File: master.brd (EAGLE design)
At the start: 160 x 100 mm, 24 parts, among them IC1 MEGA164P/324P/644P-PU, SW1 CI-11, U2 3V3 something

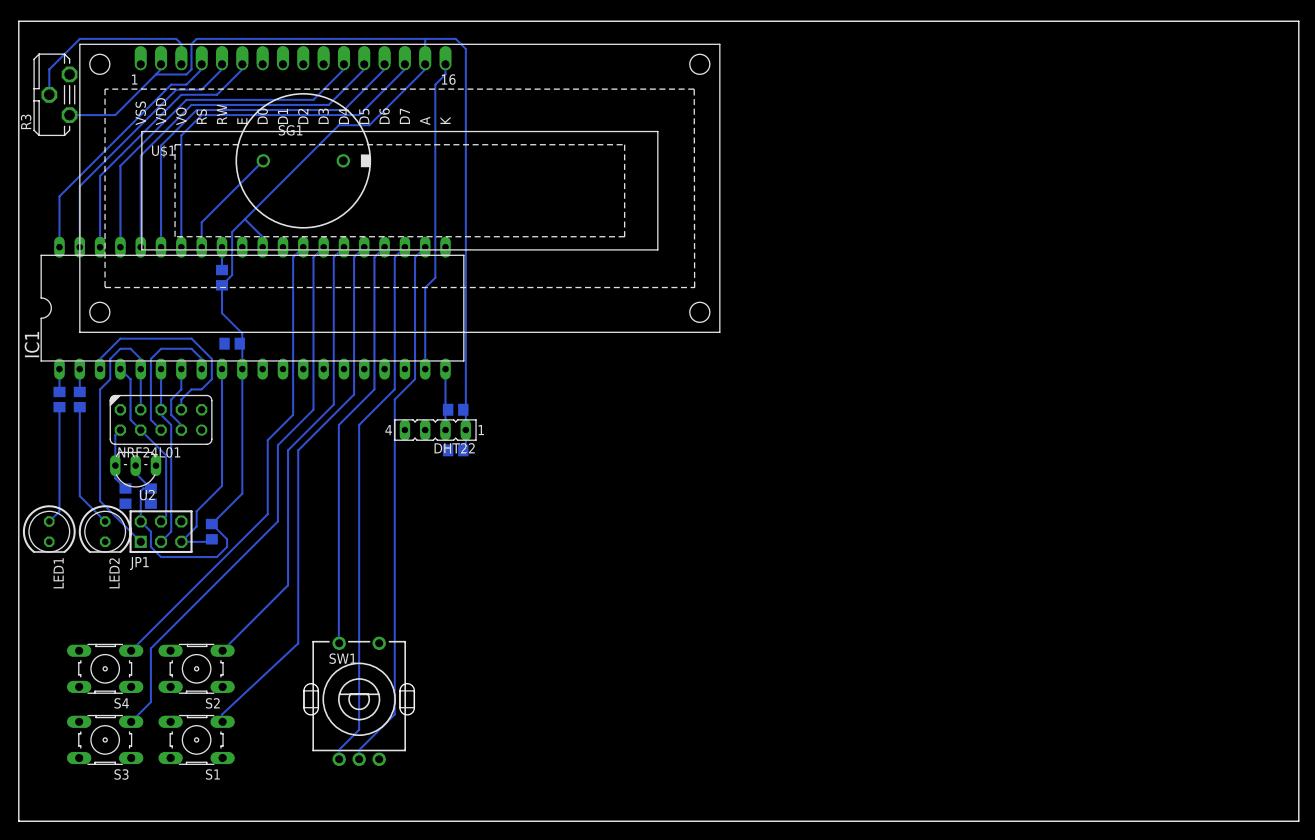
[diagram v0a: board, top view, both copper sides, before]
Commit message: added watch crystal to master, notes for sensor
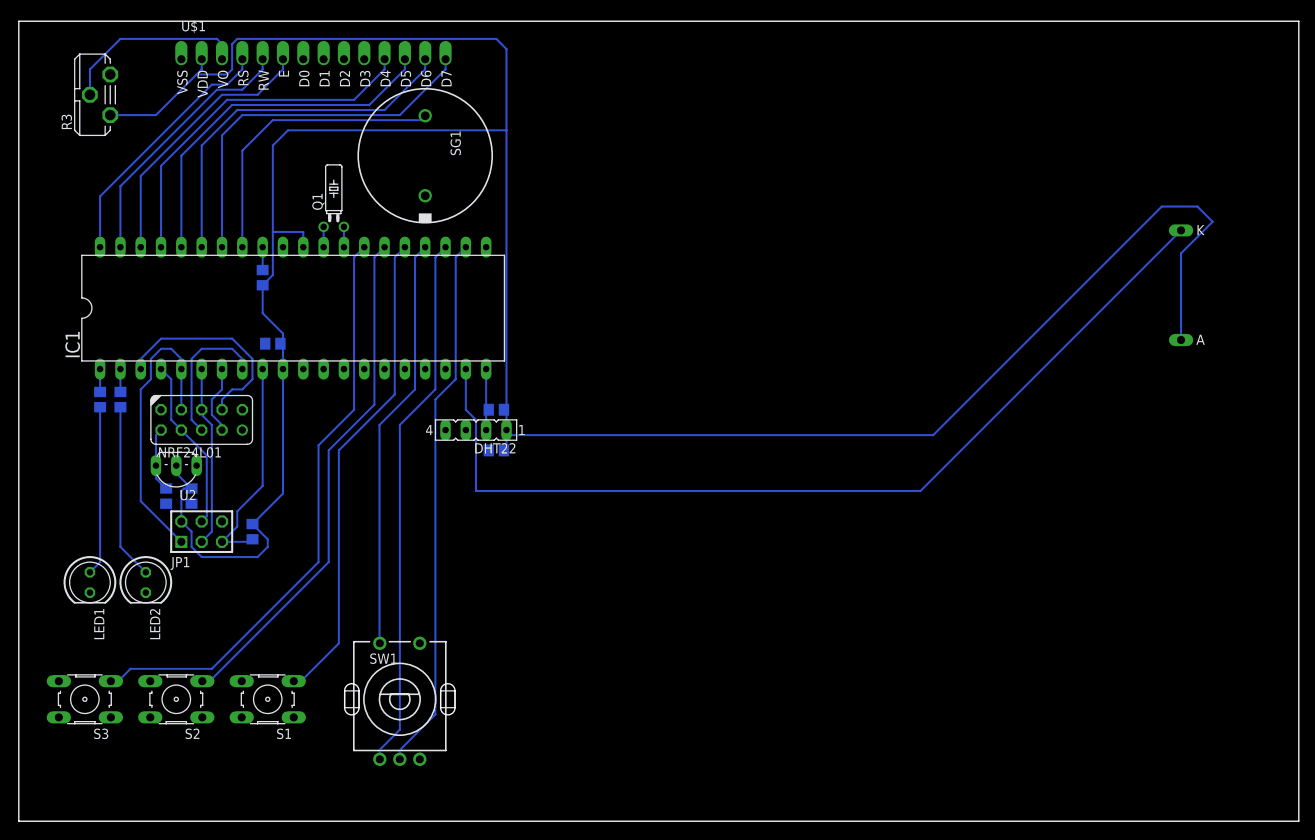
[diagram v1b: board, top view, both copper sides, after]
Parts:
- removed S4: (no value), switch-omron:B3F-10XX
- added Q1: (no value), crystal:TC26H
- U$1: value 162A -> BTHQ24008VSS; device lcd_displays:162A -> lcd_displays:BTHQ42008VSS
- moved SG1 15.3 mm to (50.8, 83.2), turned to 270 degrees
- moved S1 10.2 mm to (31.1, 15.2)
- moved U$1 8.26 mm to (2.54, 97.8)
- moved LED1 8.13 mm to (8.89, 29.8)
- moved LED2 8.13 mm to (15.9, 29.8)
- moved S3 5.68 mm to (8.26, 15.2)
- moved C2 5.08 mm to (30.5, 67.9)
- moved R1 5.08 mm to (29.2, 36.2)
- moved R3 5.08 mm to (10.2, 90.8)
- moved R4 5.08 mm to (10.2, 52.7)
- moved R5 5.08 mm to (12.7, 52.7)
- moved C1 5.08 mm to (31.8, 59.7)
- moved C3 5.08 mm to (59.7, 46.4)
- moved C7 5.08 mm to (21.6, 40.6)
- moved C8 5.08 mm to (18.4, 40.6)
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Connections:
- removed net PC6: IC1.28, S4.3
- new net N$3: IC1.29, Q1.1
- new net N$4: IC1.28, Q1.2
- net +5V: now also U$1.A, U$1.VDD; no longer U$1.15, U$1.2
- net GND: now also U$1.VSS; no longer S4.1, S4.2, U$1.1
- net N$9: now also U$1.VO; no longer U$1.3
- net PA0: now also U$1.RS; no longer U$1.4
- net PA1: now also U$1.RW; no longer U$1.5
- net PA2: now also U$1.E; no longer U$1.6
- net PA3: now also U$1.D4; no longer U$1.11
- net PA4: now also U$1.D5; no longer U$1.12
- net PA5: now also U$1.D6; no longer U$1.13
- net PA6: now also U$1.D7; no longer U$1.14
- net PD5: now also U$1.K; no longer U$1.16
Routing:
- net +5V: track 215.9 -> 339.6 mm
- net PD5: track 39.2 -> 117.4 mm
- net PC6: track 59.4 -> 0.00 mm
- net PA7: track 14.0 -> 36.7 mm
- net PC4: track 56.7 -> 64.2 mm
- net PC3: track 66.9 -> 60.5 mm
- net N$2: track 15.6 -> 22.0 mm
- net N$13: track 14.8 -> 21.2 mm
- net PC5: track 69.3 -> 73.9 mm
- net N$4: track 0.00 -> 2.54 mm
- net N$3: track 0.00 -> 2.54 mm
- net PA2: track 32.8 -> 33.5 mm
- net PA0: track 31.3 -> 32.0 mm
- net PA6: track 46.0 -> 46.6 mm
- net PA5: track 45.2 -> 45.9 mm
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
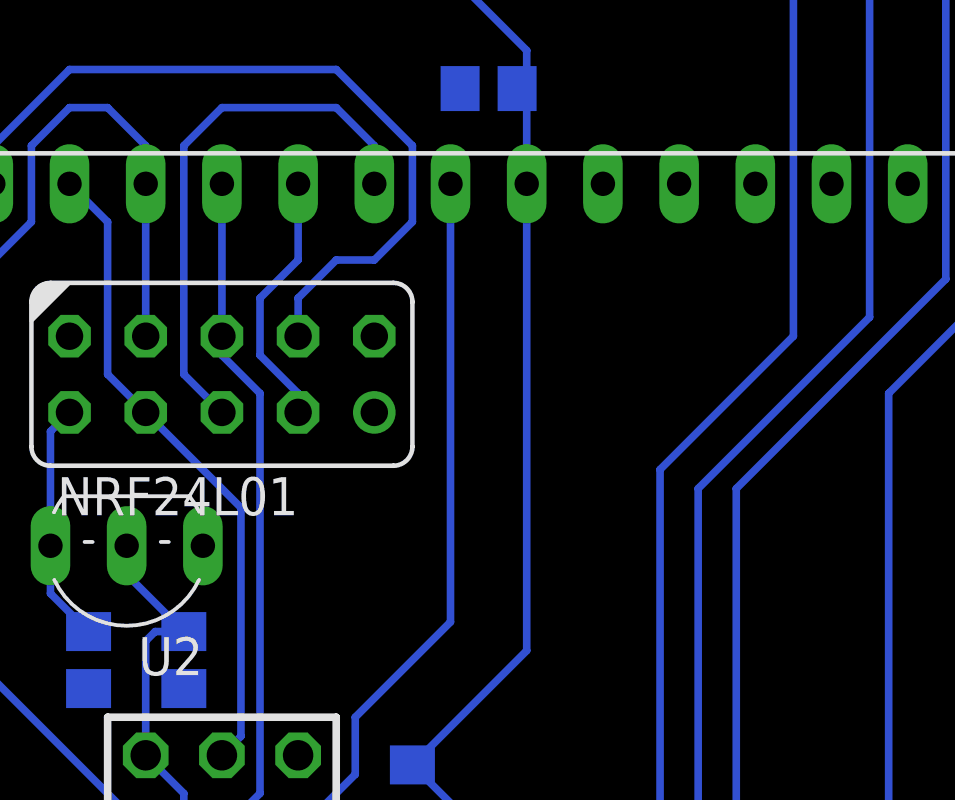
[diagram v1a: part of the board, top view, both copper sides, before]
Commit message: series resistors for shared spi/isp interface
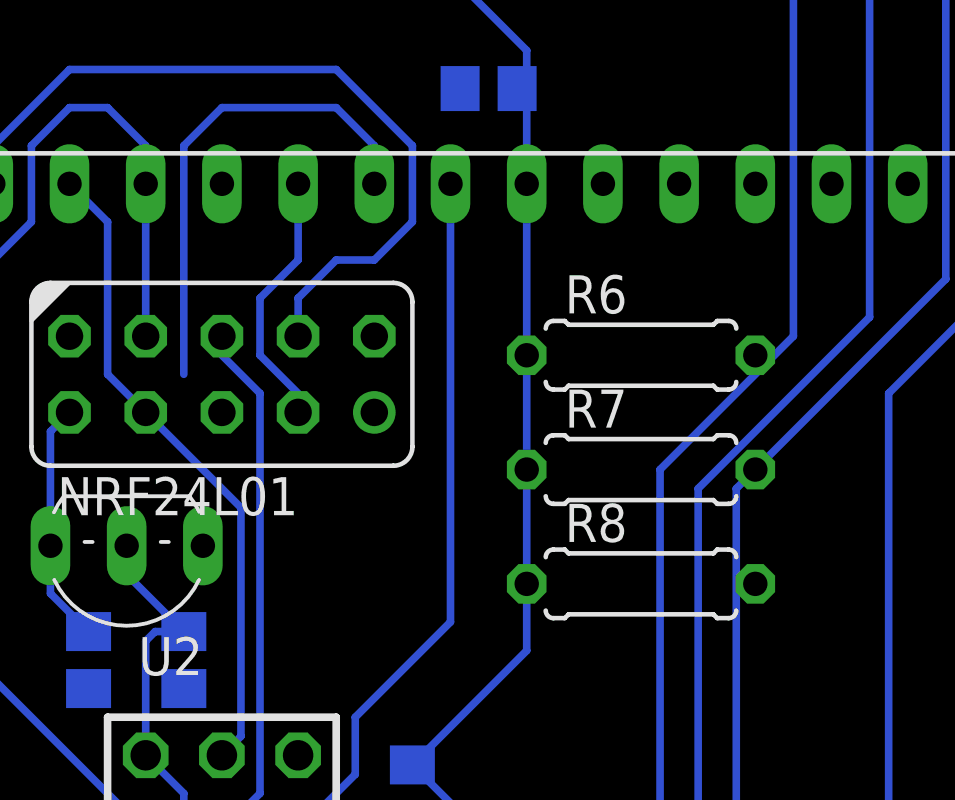
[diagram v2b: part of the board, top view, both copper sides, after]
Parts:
- added R6, R7, R8: 4k7, rcl:0207/7
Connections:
- new net N$5: NRF24L01.5, R6.2
- new net N$6: NRF24L01.3, R7.2
- new net N$7: NRF24L01.6, R8.1
- net PB5: now also R8.2; no longer NRF24L01.6
- net PB6: now also R7.1; no longer NRF24L01.3
- net PB7: now also R6.1; no longer NRF24L01.5
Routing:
- net PB5: track 22.6 -> 16.9 mm
- net PB7: track 18.1 -> 16.3 mm
- net PB6: track 8.67 -> 8.04 mm
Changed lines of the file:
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@@
 <setting verticaltext="up"/>
 </settings>
-<grid distance="0.635" unitdist="mm" unit="mm" style="lines" multiple="1" display="yes" altdistance="5" altunitdist="mil" altunit="mic"/>
+<grid distance="0.05" unitdist="inch" unit="mm" style="lines" multiple="1" display="yes" altdistance="0.025" altunitdist="inch" altunit="mm"/>
 <layers>
 <layer number="1" name="Top" color="4" fill="1" visible="yes" active="yes"/>
@@
 <attribute name="OC_REICHELT" value="0,032768-L6" x="39.37" y="74.295" size="1.778" layer="27" display="off"/>
 </element>
+<element name="R6" library="rcl" package="0207/7" value="4k7" x="36.83" y="50.8"/>
+<element name="R7" library="rcl" package="0207/7" value="4k7" x="36.83" y="46.99"/>
+<element name="R8" library="rcl" package="0207/7" value="4k7" x="36.83" y="43.18"/>
 </elements>
 <signals>
@@
 <signal name="PB5">
 <contactref element="JP1" pad="3"/>
-<contactref element="NRF24L01" pad="6"/>
 <contactref element="IC1" pad="6"/>
-<wire x1="22.86" y1="56.515" x2="22.86" y2="51.435" width="0.254" layer="16"/>
-<wire x1="22.86" y1="51.435" x2="22.86" y2="50.8" width="0.254" layer="16"/>
 <wire x1="22.86" y1="50.8" x2="24.13" y2="49.53" width="0.254" layer="16"/>
 <wire x1="24.13" y1="49.53" x2="24.13" y2="36.195" width="0.254" layer="16"/>
 <wire x1="24.13" y1="36.195" x2="22.86" y2="34.925" width="0.254" layer="16"/>
+<contactref element="R8" pad="2"/>
+<wire x1="22.86" y1="50.8" x2="22.86" y2="56.515" width="0" layer="19" extent="16-16"/>
+<wire x1="40.64" y1="43.18" x2="22.86" y2="34.925" width="0" layer="19" extent="1-1"/>
 </signal>
 <signal name="PB4">
@@
 </signal>
 <signal name="PB7">
-<contactref element="NRF24L01" pad="5"/>
 <contactref element="IC1" pad="8"/>
-<wire x1="22.86" y1="48.895" x2="21.59" y2="50.165" width="0.254" layer="16"/>
 <wire x1="21.59" y1="50.165" x2="21.59" y2="57.785" width="0.254" layer="16"/>
 <wire x1="21.59" y1="57.785" x2="22.86" y2="59.055" width="0.254" layer="16"/>
@@
 <wire x1="26.67" y1="59.055" x2="27.94" y2="57.785" width="0.254" layer="16"/>
 <wire x1="27.94" y1="57.785" x2="27.94" y2="56.515" width="0.254" layer="16"/>
+<contactref element="R6" pad="1"/>
+<wire x1="33.02" y1="50.8" x2="21.59" y2="50.165" width="0" layer="19" extent="16-16"/>
 </signal>
 <signal name="PB6">
-<contactref element="NRF24L01" pad="3"/>
 <contactref element="IC1" pad="7"/>
 <wire x1="25.4" y1="56.515" x2="25.4" y2="53.975" width="0.254" layer="16"/>
@@
 <wire x1="24.13" y1="52.705" x2="24.13" y2="50.8" width="0.254" layer="16"/>
 <wire x1="24.13" y1="50.8" x2="25.4" y2="49.53" width="0.254" layer="16"/>
-<wire x1="25.4" y1="49.53" x2="25.4" y2="48.895" width="0.254" layer="16"/>
+<contactref element="R7" pad="1"/>
+<wire x1="33.02" y1="46.99" x2="25.4" y2="49.53" width="0" layer="19" extent="16-16"/>
 </signal>
 <signal name="N$9">
@@
 <wire x1="40.64" y1="71.755" x2="40.64" y2="74.295" width="0.254" layer="16"/>
 </signal>
+<signal name="N$5">
+<contactref element="NRF24L01" pad="5"/>
+<contactref element="R6" pad="2"/>
+<wire x1="40.64" y1="50.8" x2="22.86" y2="48.895" width="0" layer="19" extent="1-1"/>
+</signal>
+<signal name="N$6">
+<contactref element="NRF24L01" pad="3"/>
+<contactref element="R7" pad="2"/>
+<wire x1="40.64" y1="46.99" x2="25.4" y2="48.895" width="0" layer="19" extent="1-1"/>
+</signal>
+<signal name="N$7">
+<contactref element="NRF24L01" pad="6"/>
+<contactref element="R8" pad="1"/>
+<wire x1="33.02" y1="43.18" x2="22.86" y2="51.435" width="0" layer="19" extent="1-1"/>
+</signal>
 </signals>

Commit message: atmega1284 is pin compatible
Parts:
- IC1: value MEGA164P/324P/644P-PU -> MEGA164/324/644/1284
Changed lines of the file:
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@@
 <element name="R1" library="rcl" package="R0805" value="10k" x="29.21" y="36.195" rot="MR90"/>
 <element name="U$1" library="lcd_displays" package="BTHQ42008VSS" value="BTHQ24008VSS" x="2.54" y="97.79"/>
-<element name="IC1" library="avr-7" package="DIL40" value="MEGA164P/324P/644P-PU" x="34.29" y="64.135"/>
+<element name="IC1" library="avr-7" package="DIL40" value="MEGA164/324/644/1284" x="34.29" y="64.135"/>
 <element name="R3" library="pot" package="ST10" value="10k" x="10.16" y="90.805" rot="R90"/>
 <element name="SG1" library="buzzer" package="EFBAA40D101" value="EFBAA40D101" x="50.8" y="83.185" rot="R270">
